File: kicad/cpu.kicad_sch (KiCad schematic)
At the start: 24 parts, among them U1 W65C816S, U2 74AC04, U3 74AC245, U4 74AC573, U5 DS1813-5+, X1 MXO45HS

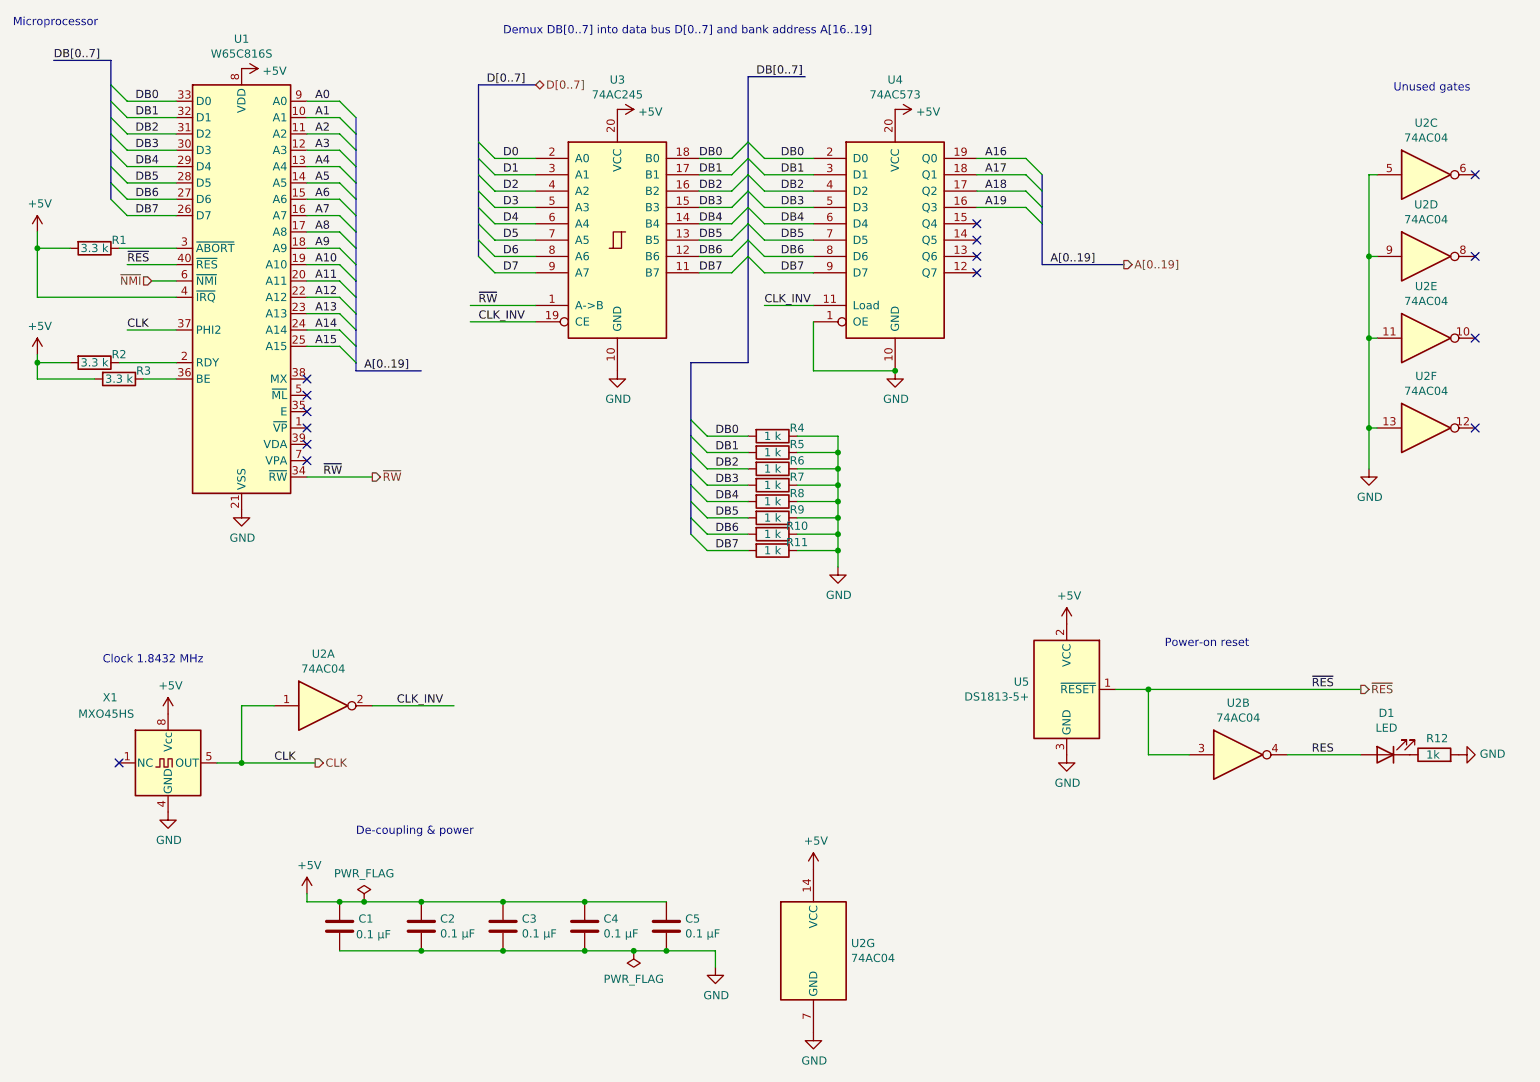
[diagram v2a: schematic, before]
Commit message: add extra 512 kB RAM, 74AC138 for future use
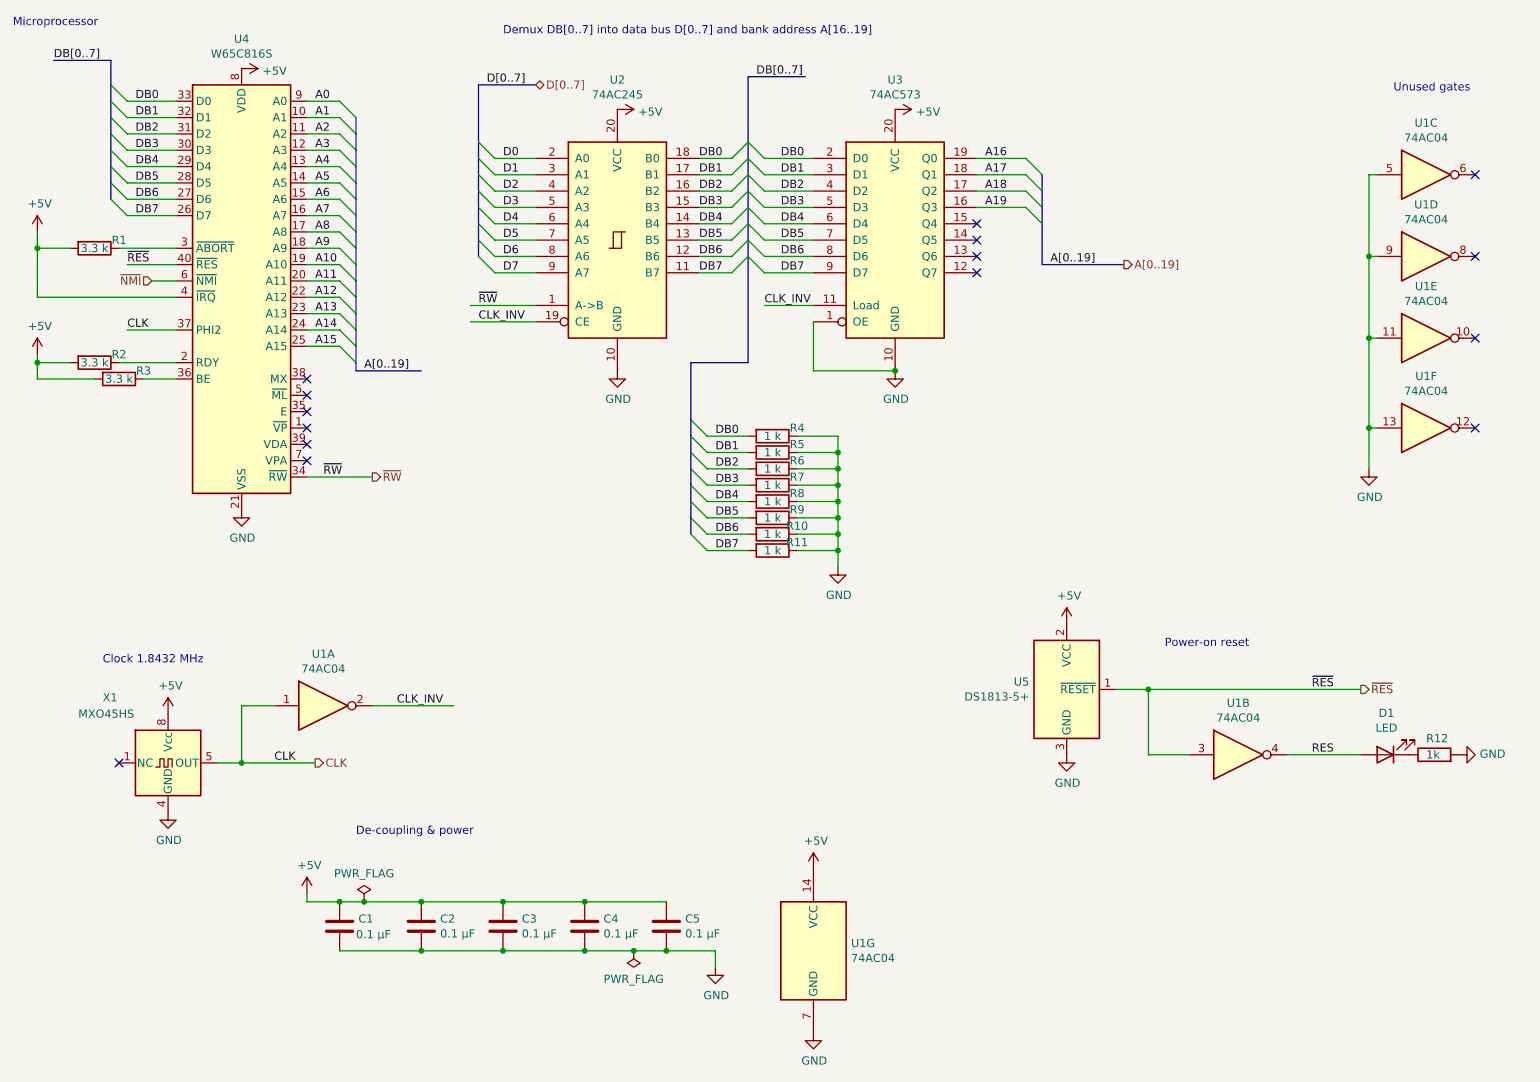
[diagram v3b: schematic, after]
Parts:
- renumbered U2 to U1, U3 to U2, U4 to U3, U1 to U4
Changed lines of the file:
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@@
   (symbol (lib_id "project:W65C816S") (at 62.23 69.85 0) (unit 1)
     (in_bom yes) (on_board yes)
-    (property "Reference" "U1" (id 0) (at 62.23 32.2326 0))
+    (property "Reference" "U4" (id 0) (at 62.23 32.2326 0))
     (property "Value" "W65C816S" (id 1) (at 62.23 34.544 0))
     (property "Footprint" "Package_DIP:DIP-40_W15.24mm" (id 2) (at 62.23 64.77 0)
@@
   (symbol (lib_id "project:74AC245") (at 120.65 63.5 0) (unit 1)
     (in_bom yes) (on_board yes)
-    (property "Reference" "U3" (id 0) (at 120.65 38.5826 0))
+    (property "Reference" "U2" (id 0) (at 120.65 38.5826 0))
     (property "Value" "74AC245" (id 1) (at 120.65 40.894 0))
     (property "Footprint" "" (id 2) (at 120.65 63.5 0)
@@
   (symbol (lib_id "project:74AC573") (at 163.83 63.5 0) (unit 1)
     (in_bom yes) (on_board yes)
-    (property "Reference" "U4" (id 0) (at 163.83 38.5826 0))
+    (property "Reference" "U3" (id 0) (at 163.83 38.5826 0))
     (property "Value" "74AC573" (id 1) (at 163.83 40.894 0))
     (property "Footprint" "" (id 2) (at 163.83 63.5 0)
@@
   (symbol (lib_id "project:74AC04") (at 74.93 135.89 0) (unit 1)
     (in_bom yes) (on_board yes)
-    (property "Reference" "U2" (id 0) (at 74.93 127.8382 0))
+    (property "Reference" "U1" (id 0) (at 74.93 127.8382 0))
     (property "Value" "74AC04" (id 1) (at 74.93 130.1496 0))
     (property "Footprint" "" (id 2) (at 74.93 135.89 0)
@@
   (symbol (lib_id "power:GND") (at 62.23 105.41 0) (unit 1)
     (in_bom yes) (on_board yes)
-    (property "Reference" "#PWR06" (id 0) (at 62.23 111.76 0)
+    (property "Reference" "#PWR09" (id 0) (at 62.23 111.76 0)
       (effects (font (size 1.27 1.27)) hide)
     )
@@
   (symbol (lib_id "power:+5V") (at 62.23 36.83 270) (unit 1)
     (in_bom yes) (on_board yes)
-    (property "Reference" "#PWR05" (id 0) (at 58.42 36.83 0)
+    (property "Reference" "#PWR01" (id 0) (at 58.42 36.83 0)
       (effects (font (size 1.27 1.27)) hide)
     )
@@
   (symbol (lib_id "power:+5V") (at 50.8 137.16 0) (unit 1)
     (in_bom yes) (on_board yes)
-    (property "Reference" "#PWR03" (id 0) (at 50.8 140.97 0)
+    (property "Reference" "#PWR012" (id 0) (at 50.8 140.97 0)
       (effects (font (size 1.27 1.27)) hide)
     )
@@
   (symbol (lib_id "power:GND") (at 50.8 152.4 0) (unit 1)
     (in_bom yes) (on_board yes)
-    (property "Reference" "#PWR04" (id 0) (at 50.8 158.75 0)
+    (property "Reference" "#PWR015" (id 0) (at 50.8 158.75 0)
       (effects (font (size 1.27 1.27)) hide)
     )
@@
   (symbol (lib_id "power:GND") (at 190.5 143.51 0) (unit 1)
     (in_bom yes) (on_board yes)
-    (property "Reference" "#PWR017" (id 0) (at 190.5 149.86 0)
+    (property "Reference" "#PWR013" (id 0) (at 190.5 149.86 0)
       (effects (font (size 1.27 1.27)) hide)
     )
@@
   (symbol (lib_id "power:GND") (at 163.83 83.82 0) (unit 1)
     (in_bom yes) (on_board yes)
-    (property "Reference" "#PWR015" (id 0) (at 163.83 90.17 0)
+    (property "Reference" "#PWR07" (id 0) (at 163.83 90.17 0)
       (effects (font (size 1.27 1.27)) hide)
     )
@@
   (symbol (lib_id "power:GND") (at 120.65 83.82 0) (unit 1)
     (in_bom yes) (on_board yes)
-    (property "Reference" "#PWR09" (id 0) (at 120.65 90.17 0)
+    (property "Reference" "#PWR06" (id 0) (at 120.65 90.17 0)
       (effects (font (size 1.27 1.27)) hide)
     )
@@
   (symbol (lib_id "power:+5V") (at 120.65 43.18 270) (unit 1)
     (in_bom yes) (on_board yes)
-    (property "Reference" "#PWR08" (id 0) (at 116.84 43.18 0)
+    (property "Reference" "#PWR02" (id 0) (at 116.84 43.18 0)
       (effects (font (size 1.27 1.27)) hide)
     )
@@
   (symbol (lib_id "power:+5V") (at 163.83 43.18 270) (unit 1)
     (in_bom yes) (on_board yes)
-    (property "Reference" "#PWR014" (id 0) (at 160.02 43.18 0)
+    (property "Reference" "#PWR03" (id 0) (at 160.02 43.18 0)
       (effects (font (size 1.27 1.27)) hide)
     )
@@
   (symbol (lib_id "power:+5V") (at 190.5 123.19 0) (unit 1)
     (in_bom yes) (on_board yes)
-    (property "Reference" "#PWR016" (id 0) (at 190.5 127 0)
+    (property "Reference" "#PWR011" (id 0) (at 190.5 127 0)
       (effects (font (size 1.27 1.27)) hide)
     )
@@
   (symbol (lib_id "power:+5V") (at 30.48 62.23 0) (unit 1)
     (in_bom yes) (on_board yes)
-    (property "Reference" "#PWR01" (id 0) (at 30.48 66.04 0)
+    (property "Reference" "#PWR04" (id 0) (at 30.48 66.04 0)
       (effects (font (size 1.27 1.27)) hide)
     )
@@
   (symbol (lib_id "power:+5V") (at 30.48 81.28 0) (unit 1)
     (in_bom yes) (on_board yes)
-    (property "Reference" "#PWR02" (id 0) (at 30.48 85.09 0)
+    (property "Reference" "#PWR05" (id 0) (at 30.48 85.09 0)
       (effects (font (size 1.27 1.27)) hide)
     )
@@
   (symbol (lib_id "project:74AC04") (at 217.17 143.51 0) (unit 2)
     (in_bom yes) (on_board yes)
-    (property "Reference" "U2" (id 0) (at 217.17 135.4582 0))
+    (property "Reference" "U1" (id 0) (at 217.17 135.4582 0))
     (property "Value" "74AC04" (id 1) (at 217.17 137.7696 0))
     (property "Footprint" "" (id 2) (at 217.17 143.51 0)
@@
   (symbol (lib_id "project:74AC04") (at 151.13 173.99 0) (unit 7)
     (in_bom yes) (on_board yes)
-    (property "Reference" "U2" (id 0) (at 156.972 172.8216 0)
+    (property "Reference" "U1" (id 0) (at 156.972 172.8216 0)
       (effects (font (size 1.27 1.27)) (justify left))
     )
@@
   (symbol (lib_id "power:PWR_FLAG") (at 123.19 173.99 180) (unit 1)
     (in_bom yes) (on_board yes)
-    (property "Reference" "#FLG0101" (id 0) (at 123.19 175.895 0)
+    (property "Reference" "#FLG02" (id 0) (at 123.19 175.895 0)
       (effects (font (size 1.27 1.27)) hide)
     )
@@
   (symbol (lib_id "project:74AC04") (at 246.38 53.34 0) (unit 3)
     (in_bom yes) (on_board yes)
-    (property "Reference" "U2" (id 0) (at 246.38 45.2882 0))
+    (property "Reference" "U1" (id 0) (at 246.38 45.2882 0))
     (property "Value" "74AC04" (id 1) (at 246.38 47.5996 0))
     (property "Footprint" "" (id 2) (at 246.38 53.34 0)
@@
   (symbol (lib_id "project:74AC04") (at 246.38 66.04 0) (unit 4)
     (in_bom yes) (on_board yes)
-    (property "Reference" "U2" (id 0) (at 246.38 57.9882 0))
+    (property "Reference" "U1" (id 0) (at 246.38 57.9882 0))
     (property "Value" "74AC04" (id 1) (at 246.38 60.2996 0))
     (property "Footprint" "" (id 2) (at 246.38 66.04 0)
@@
   (symbol (lib_id "project:74AC04") (at 246.38 78.74 0) (unit 5)
     (in_bom yes) (on_board yes)
-    (property "Reference" "U2" (id 0) (at 246.38 70.6882 0))
+    (property "Reference" "U1" (id 0) (at 246.38 70.6882 0))
     (property "Value" "74AC04" (id 1) (at 246.38 72.9996 0))
     (property "Footprint" "" (id 2) (at 246.38 78.74 0)
@@
   (symbol (lib_id "project:74AC04") (at 246.38 92.71 0) (unit 6)
     (in_bom yes) (on_board yes)
-    (property "Reference" "U2" (id 0) (at 246.38 84.6582 0))
+    (property "Reference" "U1" (id 0) (at 246.38 84.6582 0))
     (property "Value" "74AC04" (id 1) (at 246.38 86.9696 0))
     (property "Footprint" "" (id 2) (at 246.38 92.71 0)
@@
   (symbol (lib_id "power:GND") (at 237.49 99.06 0) (unit 1)
     (in_bom yes) (on_board yes)
-    (property "Reference" "#PWR018" (id 0) (at 237.49 105.41 0)
+    (property "Reference" "#PWR08" (id 0) (at 237.49 105.41 0)
       (effects (font (size 1.27 1.27)) hide)
     )
@@
   (symbol (lib_id "power:GND") (at 251.46 143.51 90) (unit 1)
     (in_bom yes) (on_board yes)
-    (property "Reference" "#PWR019" (id 0) (at 257.81 143.51 0)
+    (property "Reference" "#PWR014" (id 0) (at 257.81 143.51 0)
       (effects (font (size 1.27 1.27)) hide)
     )
@@
   (symbol (lib_id "power:+5V") (at 72.39 165.1 0) (unit 1)
     (in_bom yes) (on_board yes)
-    (property "Reference" "#PWR07" (id 0) (at 72.39 168.91 0)
+    (property "Reference" "#PWR017" (id 0) (at 72.39 168.91 0)
       (effects (font (size 1.27 1.27)) hide)
     )
@@
   (symbol (lib_id "power:GND") (at 135.89 176.53 0) (unit 1)
     (in_bom yes) (on_board yes)
-    (property "Reference" "#PWR010" (id 0) (at 135.89 182.88 0)
+    (property "Reference" "#PWR018" (id 0) (at 135.89 182.88 0)
       (effects (font (size 1.27 1.27)) hide)
     )
@@
   (symbol (lib_id "power:GND") (at 151.13 186.69 0) (unit 1)
     (in_bom yes) (on_board yes)
-    (property "Reference" "#PWR012" (id 0) (at 151.13 193.04 0)
+    (property "Reference" "#PWR019" (id 0) (at 151.13 193.04 0)
       (effects (font (size 1.27 1.27)) hide)
     )
@@
   (symbol (lib_id "power:+5V") (at 151.13 161.29 0) (unit 1)
     (in_bom yes) (on_board yes)
-    (property "Reference" "#PWR011" (id 0) (at 151.13 165.1 0)
+    (property "Reference" "#PWR016" (id 0) (at 151.13 165.1 0)
       (effects (font (size 1.27 1.27)) hide)
     )
@@
   (symbol (lib_id "power:GND") (at 154.94 114.3 0) (unit 1)
     (in_bom yes) (on_board yes)
-    (property "Reference" "#PWR013" (id 0) (at 154.94 120.65 0)
-      (effects (font (size 1.27 1.27)) hide)
-    )
+    (property "Reference" "#PWR010" (id 0) (at 154.94 120.65 0)
+      (effects (font (size 1.27 1.27)) hide)
+    )

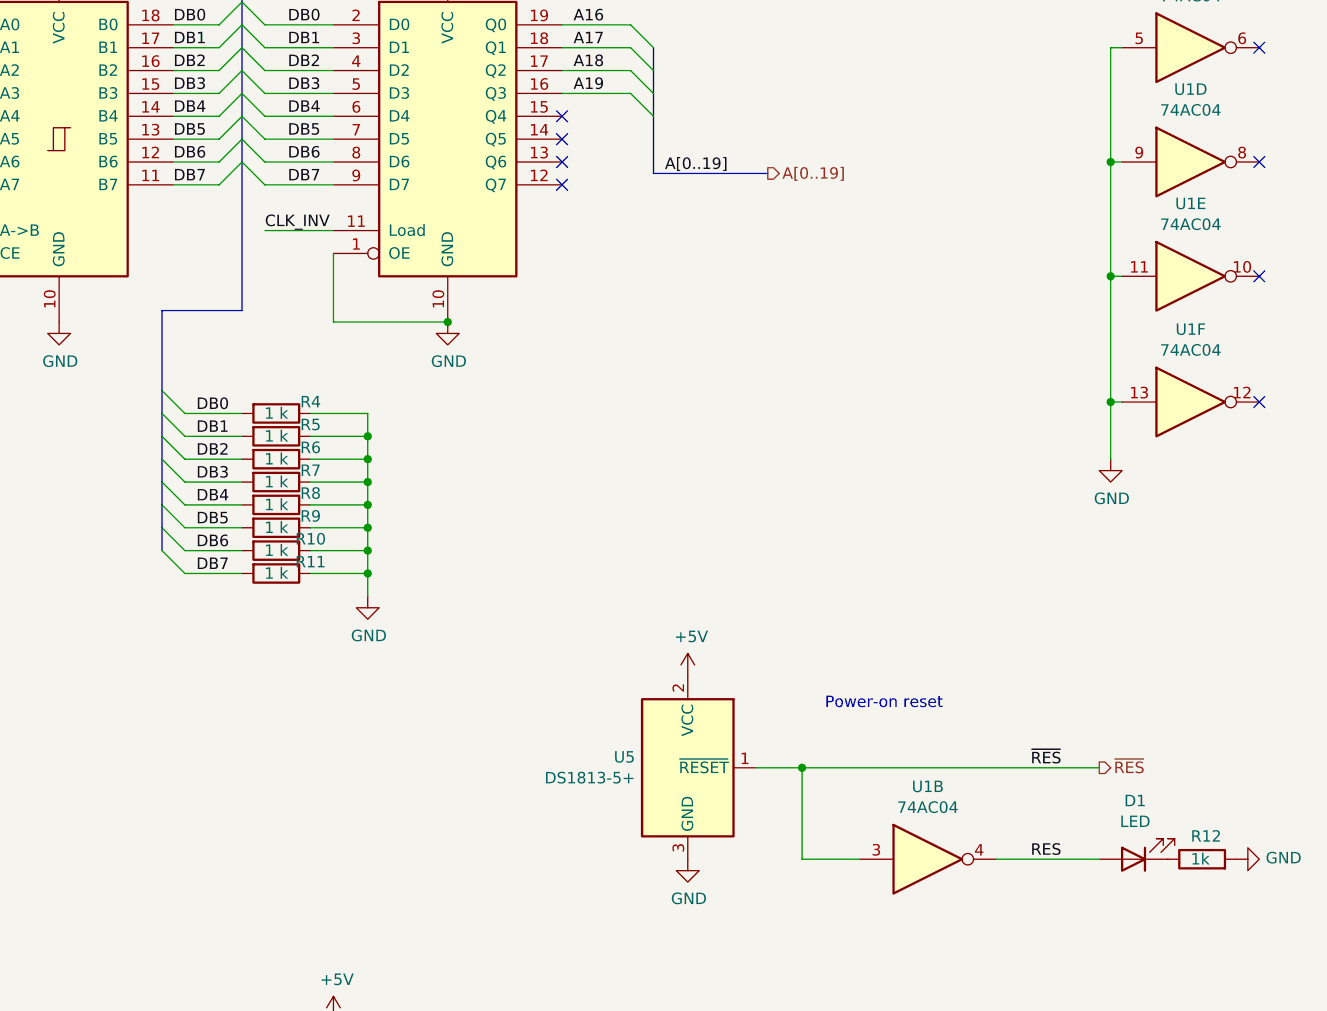
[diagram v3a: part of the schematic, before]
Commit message: separate I/O schematic page, add SC16C752 for future use
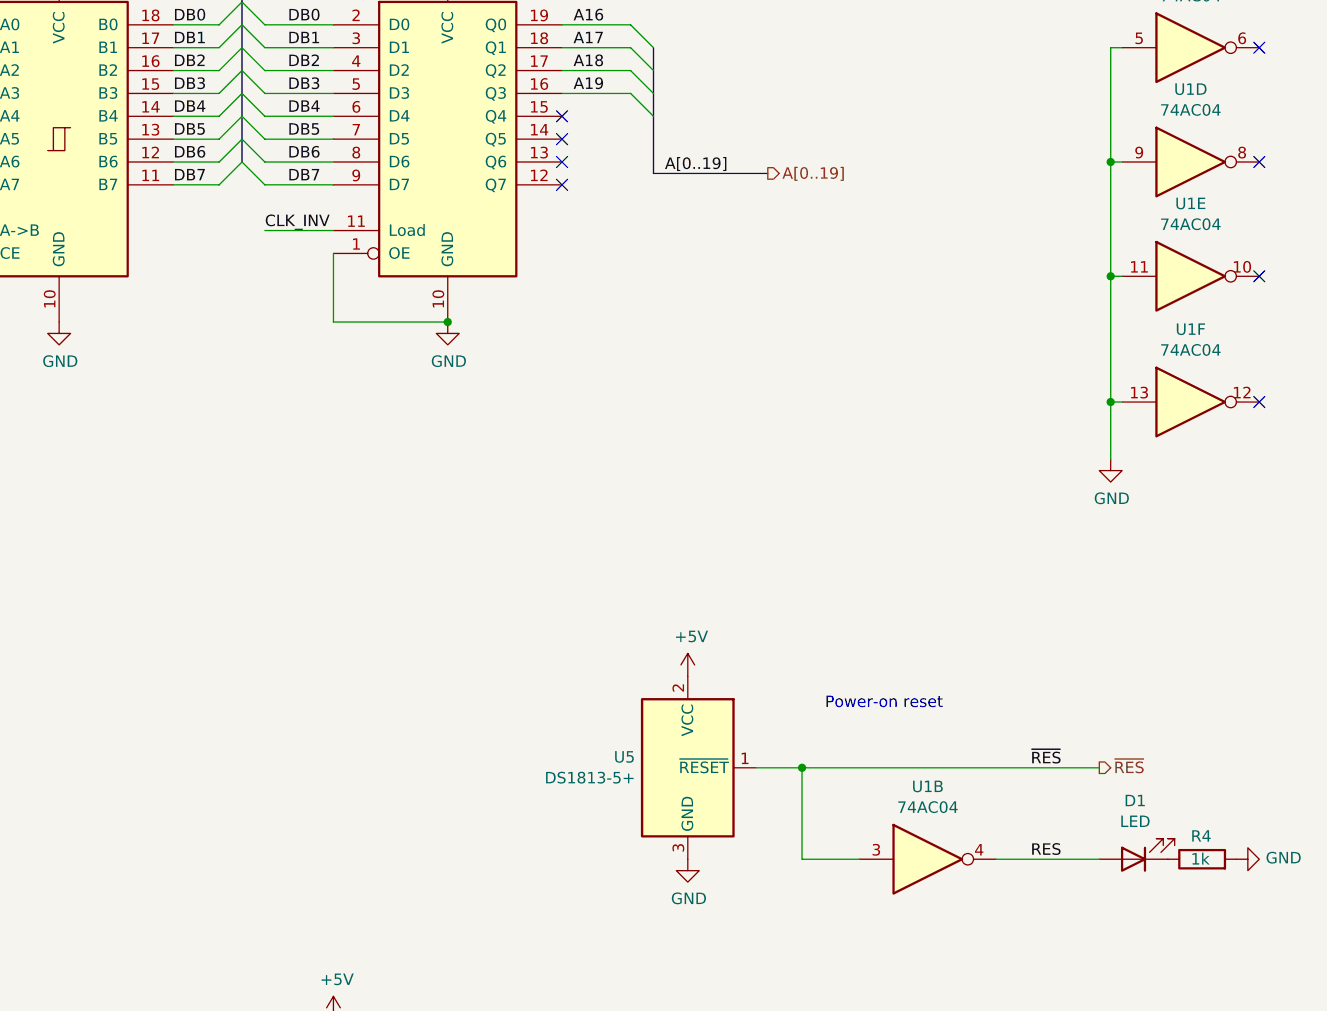
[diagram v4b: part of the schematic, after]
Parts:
- removed R10, R11, R4, R5, R6, R7, R8, R9: 1 k, symbol Device:R
- renumbered R12 to R4
